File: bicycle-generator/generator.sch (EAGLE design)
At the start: 62 parts, among them IC1 MC34063AD, K1 ARK500/2, K2 ARK500/2, K3 ARK500/2, K4 ARK500/2, K5 ARK500/2, K6 HEAT_NPN, K7 ARK500/2, K8 ARK500/2, Q1 IRF3704S, Q2 IRF3704S, T1 BC807, T2 BC807, X1 CV_LED, X2 PWR_LED, X3 5V_SW, X4 5V_LED, X5 5V_OUT

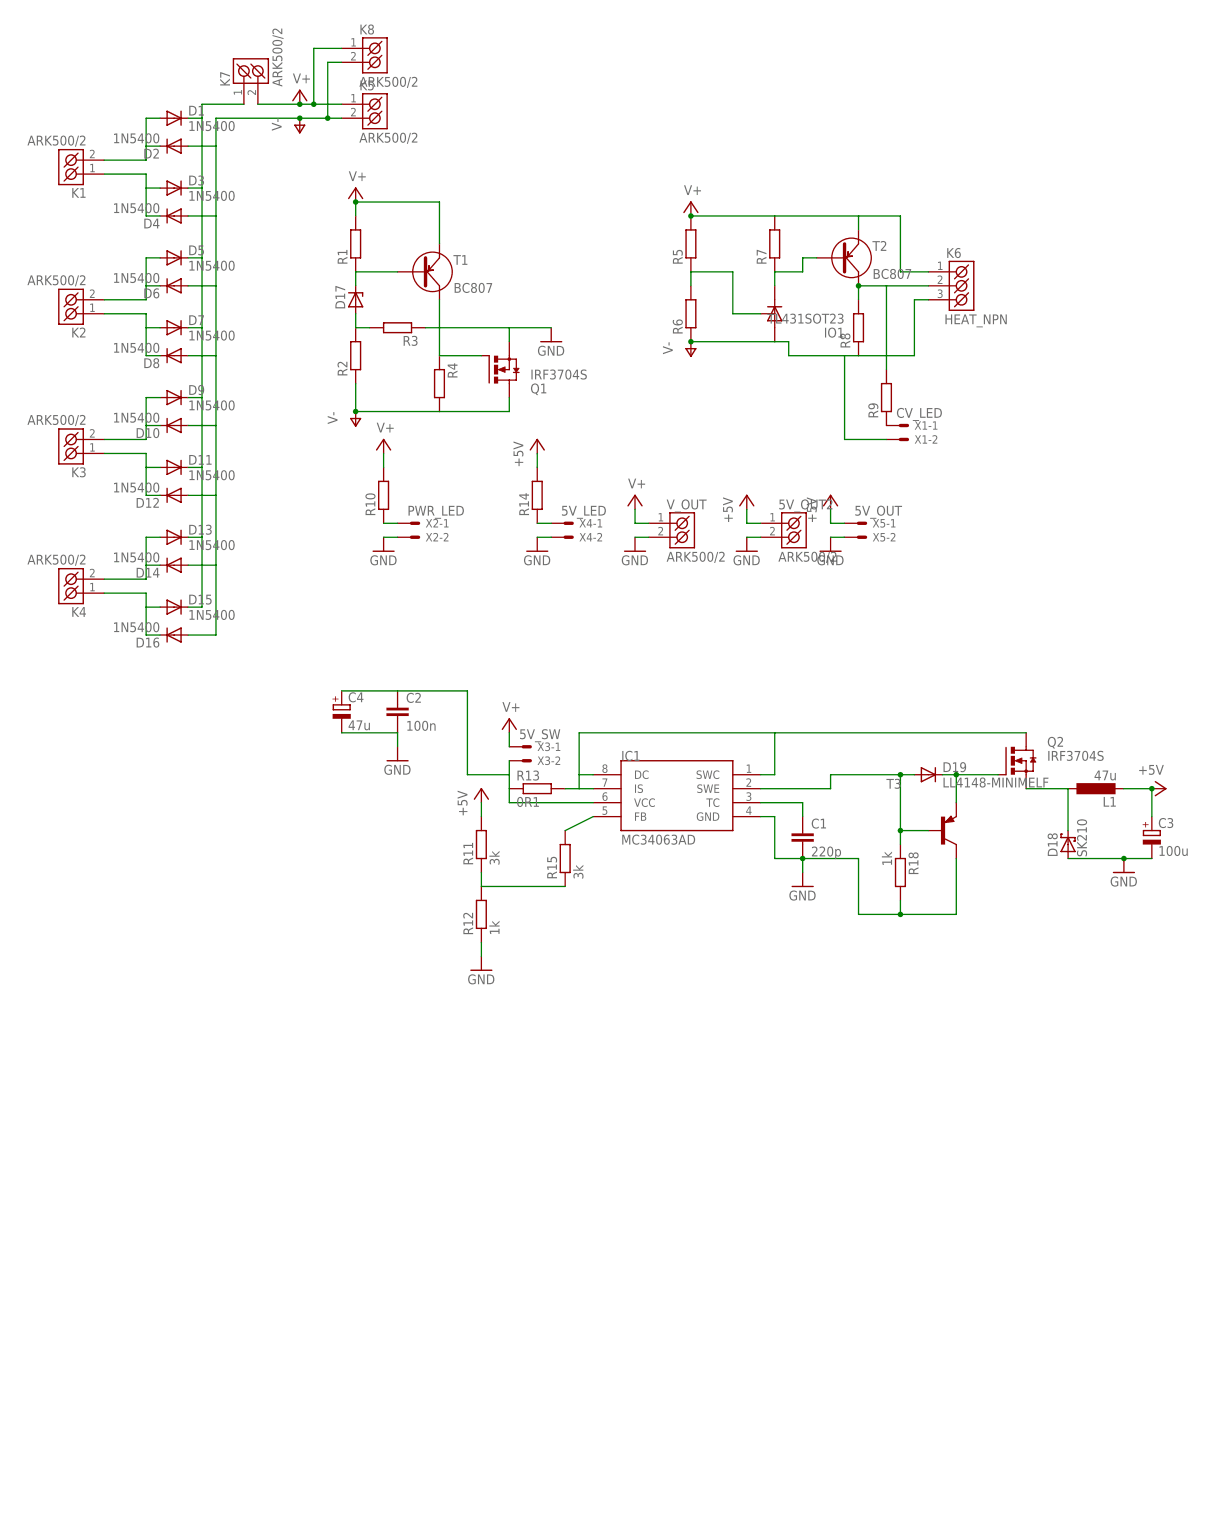
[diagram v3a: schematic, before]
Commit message: Values of parts.
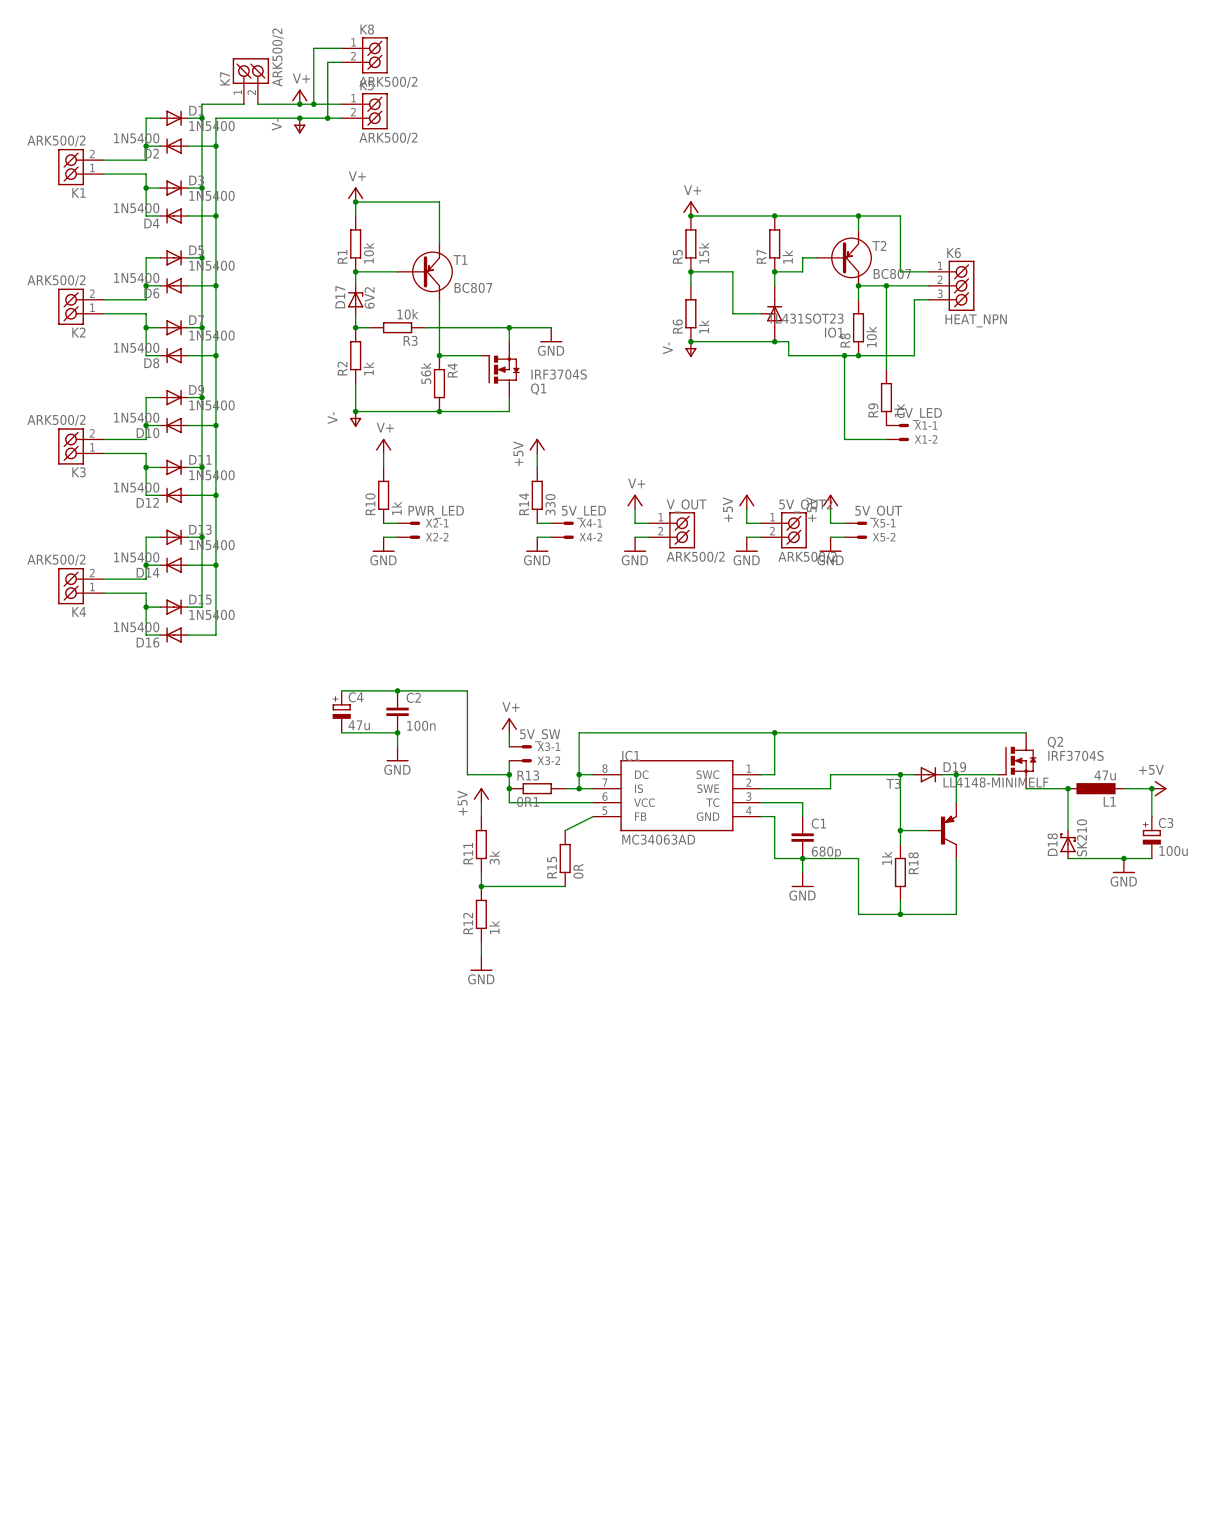
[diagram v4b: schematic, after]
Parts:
- C1: value 220p -> 680p
- D17: value (none) -> 6V2
- R1, R3, R8: value (none) -> 10k
- R10, R2, R6, R7, R9: value (none) -> 1k
- R14: value (none) -> 330
- R15: value 3k -> 0R
- R4: value (none) -> 56k
- R5: value (none) -> 15k
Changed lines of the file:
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@@
 <part name="K4" library="#PaJa_konektory" deviceset="ARK500/2" device=""/>
 <part name="K5" library="#PaJa_konektory" deviceset="ARK500/2" device=""/>
-<part name="R1" library="rcl" deviceset="R-EU_" device="R0805"/>
-<part name="R2" library="rcl" deviceset="R-EU_" device="R0805"/>
-<part name="D17" library="diode" deviceset="ZENER-DIODE" device="SOD80C"/>
+<part name="R1" library="rcl" deviceset="R-EU_" device="R0805" value="10k"/>
+<part name="R2" library="rcl" deviceset="R-EU_" device="R0805" value="1k"/>
+<part name="D17" library="diode" deviceset="ZENER-DIODE" device="SOD80C" value="6V2"/>
 <part name="T1" library="#PaJa_30" deviceset="BC807" device=""/>
 <part name="Q1" library="transistor-power" deviceset="IRF3704" device="S"/>
-<part name="R3" library="rcl" deviceset="R-EU_" device="R0805"/>
-<part name="R4" library="rcl" deviceset="R-EU_" device="R0805"/>
+<part name="R3" library="rcl" deviceset="R-EU_" device="R0805" value="10k"/>
+<part name="R4" library="rcl" deviceset="R-EU_" device="R0805" value="56k"/>
 <part name="GND2" library="supply1" deviceset="GND" device=""/>
 <part name="SUPPLY1" library="supply2" deviceset="V+" device=""/>
 <part name="SUPPLY2" library="supply2" deviceset="V+" device=""/>
 <part name="IO1" library="references" deviceset="TL431" device="SOT23"/>
-<part name="R5" library="rcl" deviceset="R-EU_" device="R0805"/>
-<part name="R6" library="rcl" deviceset="R-EU_" device="R0805"/>
-<part name="R7" library="rcl" deviceset="R-EU_" device="R0805"/>
+<part name="R5" library="rcl" deviceset="R-EU_" device="R0805" value="15k"/>
+<part name="R6" library="rcl" deviceset="R-EU_" device="R0805" value="1k"/>
+<part name="R7" library="rcl" deviceset="R-EU_" device="R0805" value="1k"/>
 <part name="K6" library="#PaJa_konektory" deviceset="ARK500/3" device="" value="HEAT_NPN"/>
 <part name="P-1" library="supply1" deviceset="V-" device=""/>
 <part name="P-2" library="supply1" deviceset="V-" device=""/>
 <part name="SUPPLY3" library="supply2" deviceset="V+" device=""/>
-<part name="R8" library="rcl" deviceset="R-EU_" device="R0805"/>
+<part name="R8" library="rcl" deviceset="R-EU_" device="R0805" value="10k"/>
 <part name="T2" library="#PaJa_30" deviceset="BC807" device=""/>
 <part name="X1" library="con-molex" deviceset="22-23-2021" device="" value="CV_LED"/>
 <part name="X2" library="con-molex" deviceset="22-23-2021" device="" value="PWR_LED"/>
-<part name="R9" library="rcl" deviceset="R-EU_" device="R0805"/>
-<part name="R10" library="rcl" deviceset="R-EU_" device="R0805"/>
+<part name="R9" library="rcl" deviceset="R-EU_" device="R0805" value="1k"/>
+<part name="R10" library="rcl" deviceset="R-EU_" device="R0805" value="1k"/>
 <part name="IC1" library="mc34063" deviceset="MC34063" device="AD"/>
 <part name="GND3" library="supply1" deviceset="GND" device=""/>
 <part name="P+2" library="supply1" deviceset="+5V" device=""/>
-<part name="C1" library="rcl" deviceset="C-EU" device="C0805" value="220p"/>
+<part name="C1" library="rcl" deviceset="C-EU" device="C0805" value="680p"/>
 <part name="R11" library="rcl" deviceset="R-EU_" device="R0805" value="3k"/>
 <part name="R12" library="rcl" deviceset="R-EU_" device="R0805" value="1k"/>
@@
 <part name="GND11" library="supply1" deviceset="GND" device=""/>
 <part name="X3" library="con-molex" deviceset="22-23-2021" device="" value="5V_SW"/>
-<part name="R14" library="rcl" deviceset="R-EU_" device="R0805"/>
+<part name="R14" library="rcl" deviceset="R-EU_" device="R0805" value="330"/>
 <part name="X4" library="con-molex" deviceset="22-23-2021" device="" value="5V_LED"/>
 <part name="GND1" library="supply1" deviceset="GND" device=""/>
@@
 <part name="P+5" library="supply1" deviceset="+5V" device=""/>
 <part name="GND9" library="supply1" deviceset="GND" device=""/>
-<part name="R15" library="rcl" deviceset="R-EU_" device="R1206" value="3k"/>
+<part name="R15" library="rcl" deviceset="R-EU_" device="R1206" value="0R"/>
 <part name="R18" library="resistor" deviceset="R-EU_" device="R0805" value="1k"/>
 <part name="D19" library="diode" deviceset="PMLL41*" device="SOD80C" value="LL4148-MINIMELF"/>
@@
 <pinref part="D2" gate="1" pin="C"/>
 <wire x1="12.7" y1="78.74" x2="10.16" y2="78.74" width="0.1524" layer="91"/>
+<junction x="10.16" y="78.74"/>
 </segment>
 </net>
@@
 <pinref part="D3" gate="1" pin="A"/>
 <wire x1="12.7" y1="71.12" x2="10.16" y2="71.12" width="0.1524" layer="91"/>
+<junction x="10.16" y="71.12"/>
 </segment>
 </net>
@@
 <pinref part="D6" gate="1" pin="C"/>
 <wire x1="12.7" y1="53.34" x2="10.16" y2="53.34" width="0.1524" layer="91"/>
+<junction x="10.16" y="53.34"/>
 </segment>
 </net>
@@
 <pinref part="D7" gate="1" pin="A"/>
 <wire x1="12.7" y1="45.72" x2="10.16" y2="45.72" width="0.1524" layer="91"/>
+<junction x="10.16" y="45.72"/>
 </segment>
 </net>
@@
 <pinref part="D10" gate="1" pin="C"/>
 <wire x1="12.7" y1="27.94" x2="10.16" y2="27.94" width="0.1524" layer="91"/>
+<junction x="10.16" y="27.94"/>
 </segment>
 </net>
@@
 <pinref part="D11" gate="1" pin="A"/>
 <wire x1="12.7" y1="20.32" x2="10.16" y2="20.32" width="0.1524" layer="91"/>
+<junction x="10.16" y="20.32"/>
 </segment>
 </net>
@@
 <pinref part="D14" gate="1" pin="C"/>
 <wire x1="12.7" y1="2.54" x2="10.16" y2="2.54" width="0.1524" layer="91"/>
+<junction x="10.16" y="2.54"/>
 </segment>
 </net>
@@
 <pinref part="D15" gate="1" pin="A"/>
 <wire x1="12.7" y1="-5.08" x2="10.16" y2="-5.08" width="0.1524" layer="91"/>
+<junction x="10.16" y="-5.08"/>
 </segment>
 </net>
@@
 <pinref part="T1" gate="T" pin="B"/>
 <wire x1="48.26" y1="55.88" x2="55.88" y2="55.88" width="0.1524" layer="91"/>
+<junction x="48.26" y="55.88"/>
 </segment>
 </net>
@@
 <pinref part="R3" gate="G$1" pin="2"/>
 <wire x1="48.26" y1="45.72" x2="50.8" y2="45.72" width="0.1524" layer="91"/>
+<junction x="48.26" y="45.72"/>
 </segment>
 </net>
@@
 <pinref part="T1" gate="T" pin="C"/>
 <wire x1="63.5" y1="40.64" x2="63.5" y2="50.8" width="0.1524" layer="91"/>
+<junction x="63.5" y="40.64"/>
 </segment>
 </net>
@@
 <wire x1="139.7" y1="63.5" x2="139.7" y2="66.04" width="0.1524" layer="91"/>
 <pinref part="T2" gate="T" pin="E"/>
+<junction x="139.7" y="66.04"/>
+<junction x="124.46" y="66.04"/>
 </segment>
 <segment>
@@
 <wire x1="129.54" y1="58.42" x2="132.08" y2="58.42" width="0.1524" layer="91"/>
 <pinref part="T2" gate="T" pin="B"/>
+<junction x="124.46" y="55.88"/>
 </segment>
 </net>
@@
 <wire x1="76.2" y1="45.72" x2="83.82" y2="45.72" width="0.1524" layer="91"/>
 <pinref part="GND2" gate="1" pin="GND"/>
+<junction x="76.2" y="45.72"/>
 </segment>
 <segment>
@@
 <pinref part="C4" gate="G$1" pin="-"/>
 <wire x1="45.72" y1="-27.94" x2="55.88" y2="-27.94" width="0.1524" layer="91"/>
+<junction x="55.88" y="-27.94"/>
 </segment>
 <segment>
@@
 <pinref part="P-1" gate="1" pin="V-"/>
 <junction x="48.26" y="30.48"/>
+<junction x="63.5" y="30.48"/>
 </segment>
 <segment>
@@
 <wire x1="43.18" y1="93.98" x2="43.18" y2="83.82" width="0.1524" layer="91"/>
 <junction x="43.18" y="83.82"/>
+<junction x="22.86" y="78.74"/>
+<junction x="22.86" y="66.04"/>
+<junction x="22.86" y="53.34"/>
+<junction x="22.86" y="40.64"/>
+<junction x="22.86" y="2.54"/>
+<junction x="22.86" y="15.24"/>
+<junction x="22.86" y="27.94"/>
 </segment>
 <segment>
@@
 <pinref part="P-3" gate="1" pin="V-"/>
 <junction x="109.22" y="43.18"/>
+<junction x="124.46" y="43.18"/>
+<junction x="137.16" y="40.64"/>
+<junction x="139.7" y="40.64"/>
 </segment>
 </net>
@@
 <pinref part="IO1" gate="G$1" pin="R"/>
 <wire x1="116.84" y1="48.26" x2="121.92" y2="48.26" width="0.1524" layer="91"/>
+<junction x="109.22" y="55.88"/>
 </segment>
 </net>
@@
 <wire x1="144.78" y1="53.34" x2="144.78" y2="38.1" width="0.1524" layer="91"/>
 <pinref part="R9" gate="G$1" pin="2"/>
+<junction x="144.78" y="53.34"/>
 </segment>
 </net>
@@
 <wire x1="71.12" y1="-55.88" x2="86.36" y2="-55.88" width="0.1524" layer="91"/>
 <pinref part="R15" gate="G$1" pin="1"/>
+<junction x="71.12" y="-55.88"/>
 </segment>
 </net>
@@
 <wire x1="177.8" y1="-38.1" x2="170.18" y2="-38.1" width="0.1524" layer="91"/>
 <pinref part="Q2" gate="G$1" pin="S"/>
+<junction x="177.8" y="-38.1"/>
 </segment>
 </net>
@@
 <pinref part="K7" gate="K" pin="K1"/>
 <wire x1="20.32" y1="86.36" x2="27.94" y2="86.36" width="0.1524" layer="91"/>
+<junction x="20.32" y="83.82"/>
+<junction x="20.32" y="71.12"/>
+<junction x="20.32" y="58.42"/>
+<junction x="20.32" y="45.72"/>
+<junction x="20.32" y="7.62"/>
+<junction x="20.32" y="20.32"/>
+<junction x="20.32" y="33.02"/>
 </segment>
 </net>
@@
 <wire x1="76.2" y1="-35.56" x2="76.2" y2="-33.02" width="0.1524" layer="91"/>
 <wire x1="68.58" y1="-35.56" x2="76.2" y2="-35.56" width="0.1524" layer="91"/>
+<junction x="76.2" y="-35.56"/>
+<junction x="76.2" y="-38.1"/>
+<junction x="55.88" y="-20.32"/>
 </segment>
 </net>
@@
 <wire x1="124.46" y1="-27.94" x2="170.18" y2="-27.94" width="0.1524" layer="91"/>
 <pinref part="Q2" gate="G$1" pin="D"/>
-</segment>
-</net>
+<junction x="124.46" y="-27.94"/>
+<junction x="88.9" y="-38.1"/>
+<junction x="88.9" y="-35.56"/>
+</segment>
+</net>
